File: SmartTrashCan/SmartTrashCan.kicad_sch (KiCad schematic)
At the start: 36 parts, among them J1 USB_C_Receptacle_USB2.0_16P, J2 USB_C_Receptacle_USB2.0_16P, SW1 SW_Push, SW2 SW_Push, U1 ESP32-C6-WROOM-1, U2 AZ1117-3.3, U3 CP2102N-Axx-xQFN20

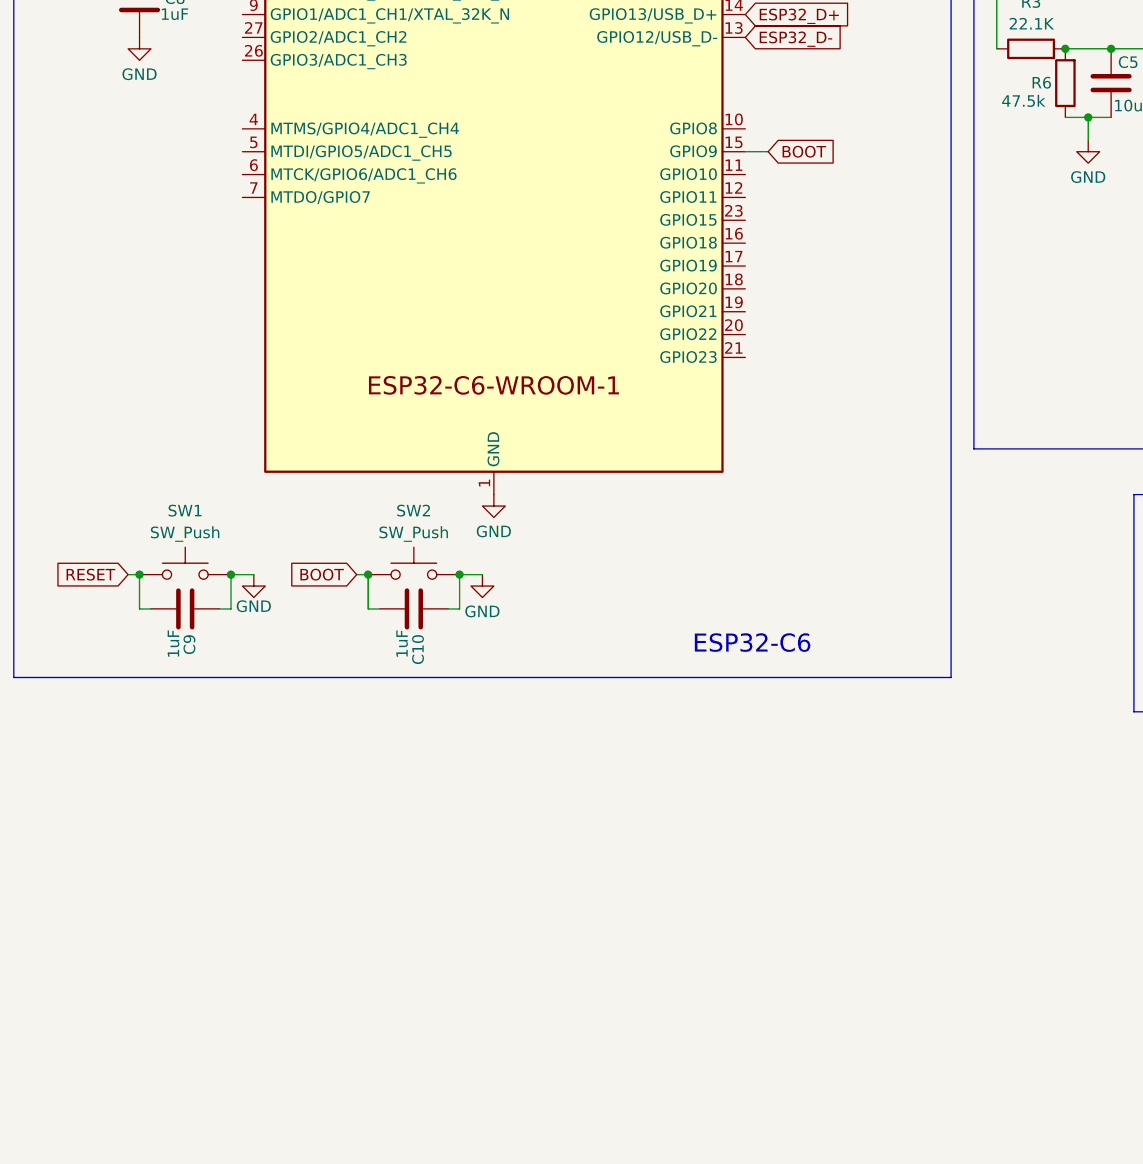
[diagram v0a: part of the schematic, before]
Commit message: Replaced projects
Deleted personal projects, and added just projects by name.
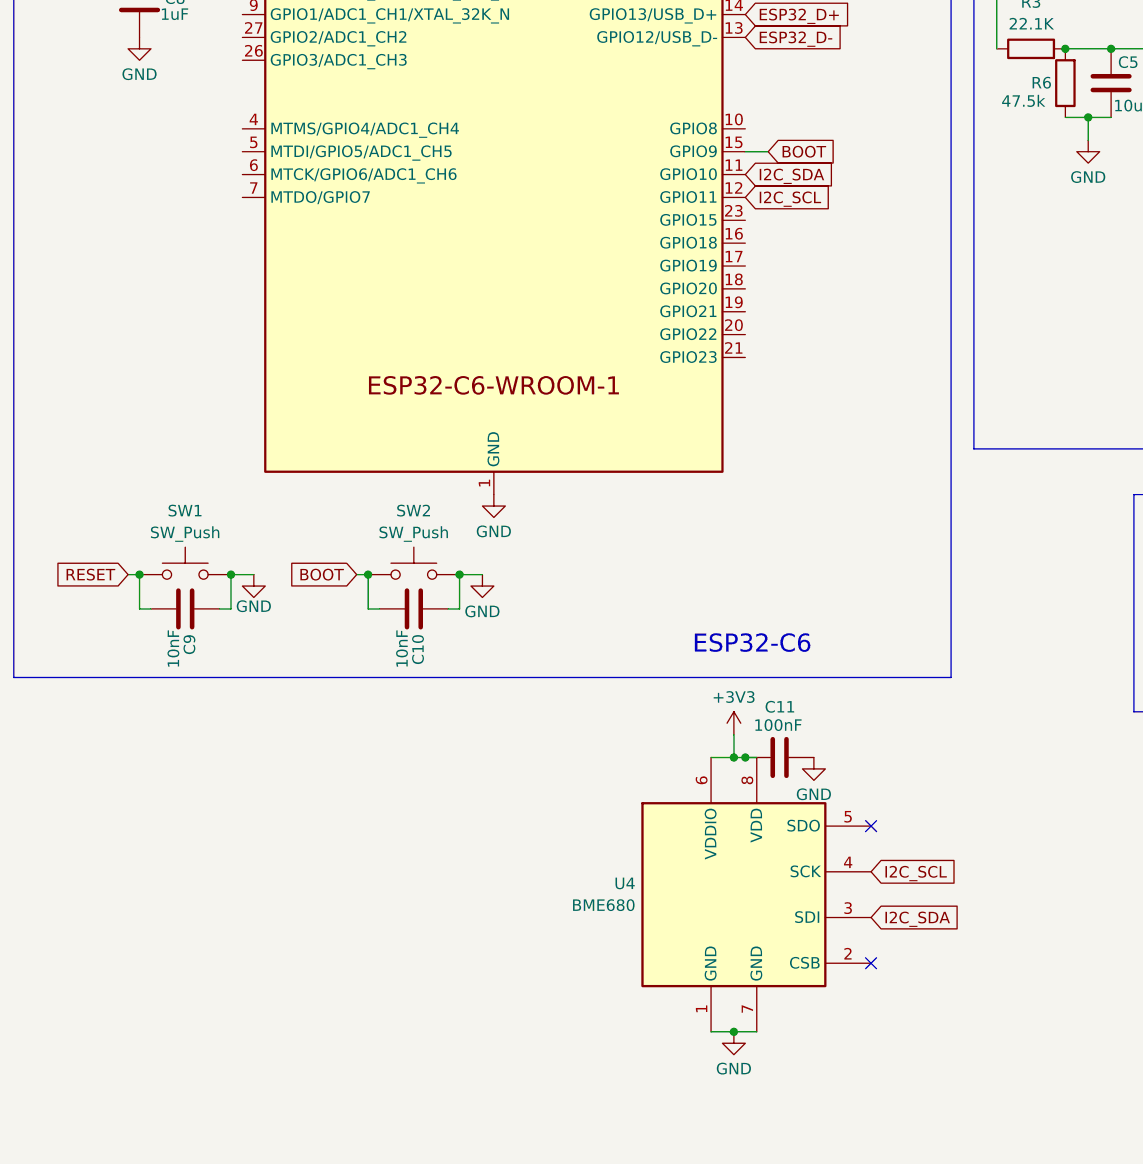
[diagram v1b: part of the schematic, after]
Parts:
- added C11: 100nF, symbol Device:C
- added U4: BME680, Package_LGA:Bosch_LGA-8_3x3mm_P0.8mm_ClockwisePinNumbering, symbol Sensor:BME680
- C10, C9: value 1uF -> 10nF
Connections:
- net +3V3: now also C11.1, U4.6 (VDDIO), U4.8 (VDD)
- net GND: now also C11.2, U4.1 (GND), U4.7 (GND)
- net I2C_SDA: now reaches U1.11 (GPIO10)
- net I2C_SDA: now also U4.3 (SDI)
- net I2C_SCL: now reaches U1.12 (GPIO11)
- net I2C_SCL: now also U4.4 (SCK)
- no-connect marks 12 -> 14
